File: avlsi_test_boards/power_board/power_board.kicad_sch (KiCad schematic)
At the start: 4 parts, among them J1 2171750001, J2 2171750001, J3 Conn_01x02_Pin, J4 Conn_01x02_Pin

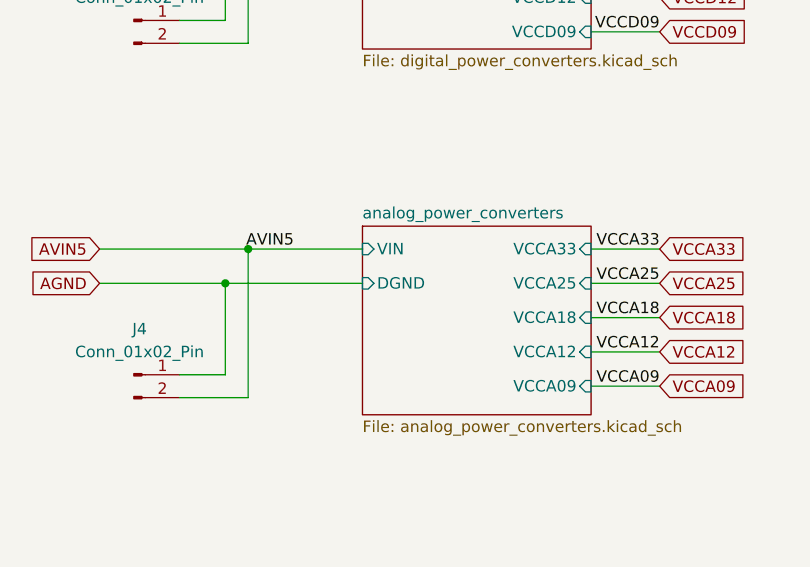
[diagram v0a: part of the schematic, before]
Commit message: Add power board
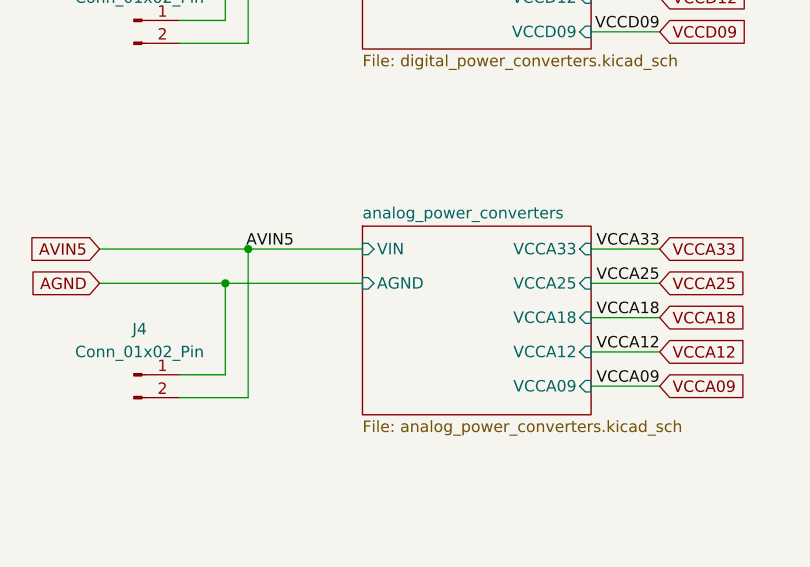
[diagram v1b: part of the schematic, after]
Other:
- sheet analog_power_converters ports: added AGND; removed DGND
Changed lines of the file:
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@@
 			)
 		)
-		(pin "DGND" input
+		(pin "AGND" input
 			(at 156.21 67.31 180)
 			(effects
